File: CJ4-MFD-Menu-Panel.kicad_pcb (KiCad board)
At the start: 2 copper layers, 122.4 x 62.5 mm, 76 parts, among them J1 USB_B_Mini, J2 AVR-ISP-6, SW1 SW_Push_LED, SW10 5_Way_Switch, SW11 SW_Push_LED, SW12 SW_Push_LED, SW13 SW_Push_LED, SW14 SW_Push_LED, SW15 SW_Push_LED, SW16 SW_Push_LED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

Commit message: Miscellaneous fixes
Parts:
- C16, C17, C18, C19, C20, C21, C22, C23, C24, C25, C26, C27, R11, R12, R14, R15, R19, R21: footprint Collins-FMS-3000:Perfect_0402 -> CJ4-MFD-Menu-Panel:Perfect_0402
- D1: footprint Collins-FMS-3000:LED_0603_1608Metric -> LED_SMD:LED_0805_2012Metric_Pad1.15x1.40mm_HandSolder
- J1: footprint Collins-FMS-3000:USB_B_Mini_Amphenol_UE25BE5510H -> CJ4-MFD-Menu-Panel:USB_B_Mini_Amphenol_UE25BE5510H
- moved D1 0.25 mm to (148.8, 27.7)
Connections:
- U4 pad 37: UP -> DOWN
- U4 pad 39: DOWN -> UP

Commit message: PCB generation is failing due to date replacement Fixes #11
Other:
- board text added: "%%date%%"
- board text added: "%%version%%"
- board text removed: "%%version%% %%date%%"

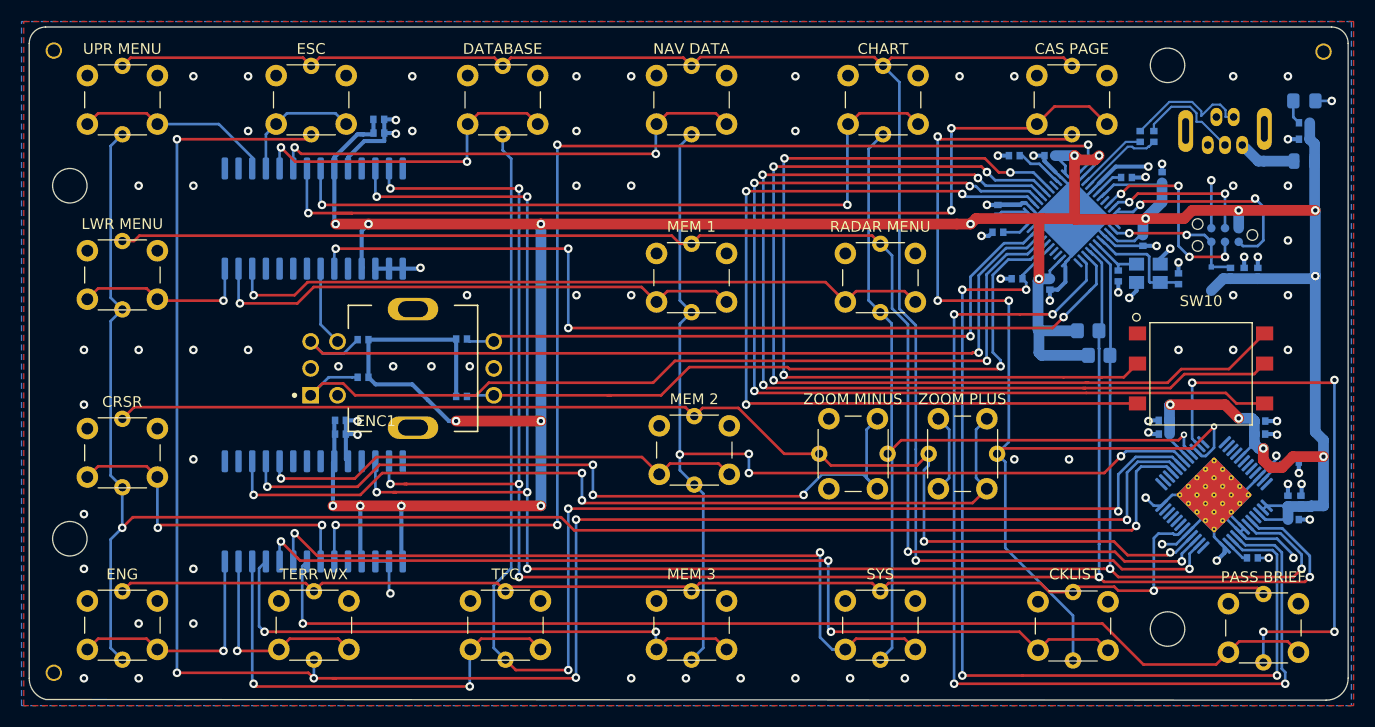
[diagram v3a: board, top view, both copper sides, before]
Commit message: Update to KiCad 6, update 3D models
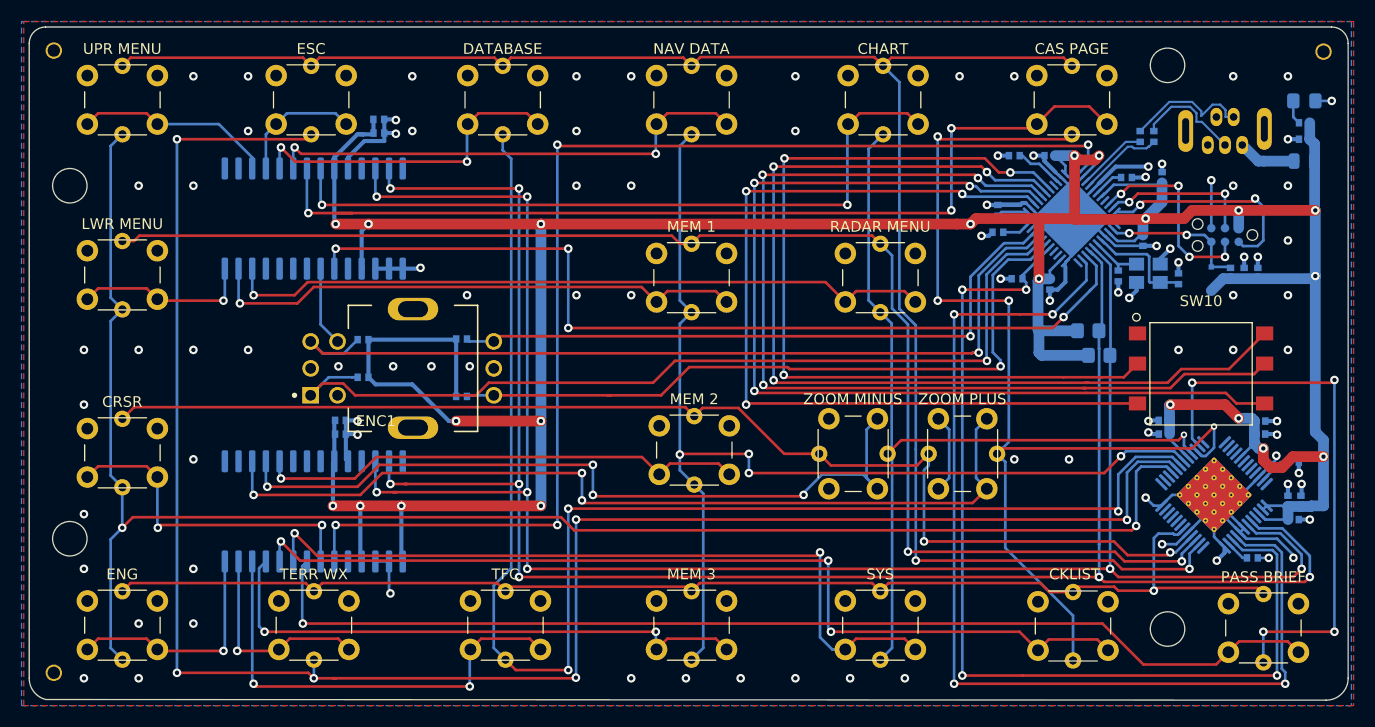
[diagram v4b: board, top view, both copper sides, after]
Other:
- net class Default removed
